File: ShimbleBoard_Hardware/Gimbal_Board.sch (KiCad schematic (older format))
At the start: 84 parts, among them Q1 Q_NMOS_GDS, Q2 Q_NMOS_GDS, Q3 Q_NMOS_GDS, Q4 Q_NMOS_GDS, Q5 Q_NMOS_GDS, Q6 Q_NMOS_GDS, Q7 Q_NMOS_GDS, Q8 Q_NMOS_GDS, SW1 SW_Push, SW10 SW_SPDT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

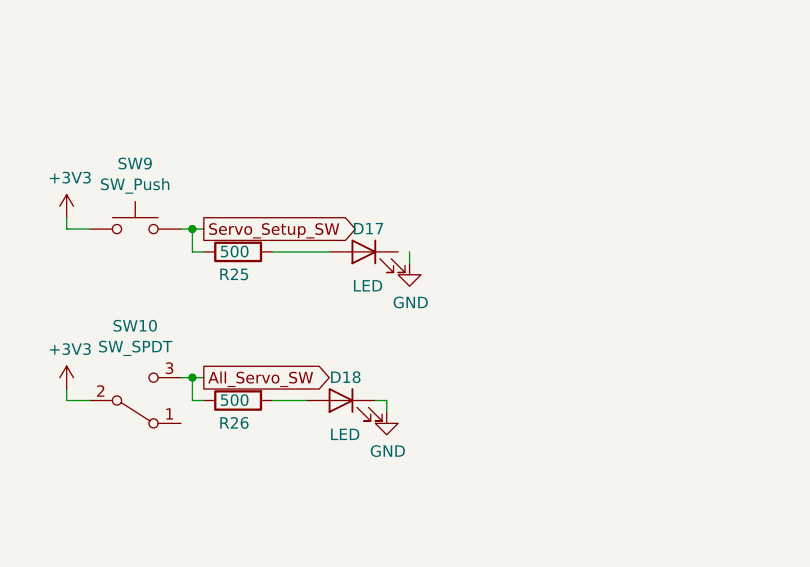
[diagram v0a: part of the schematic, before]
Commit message: PCB placement (not finished
PCB component placement and wiring
Still needs a lot more work, button pins need to be determined
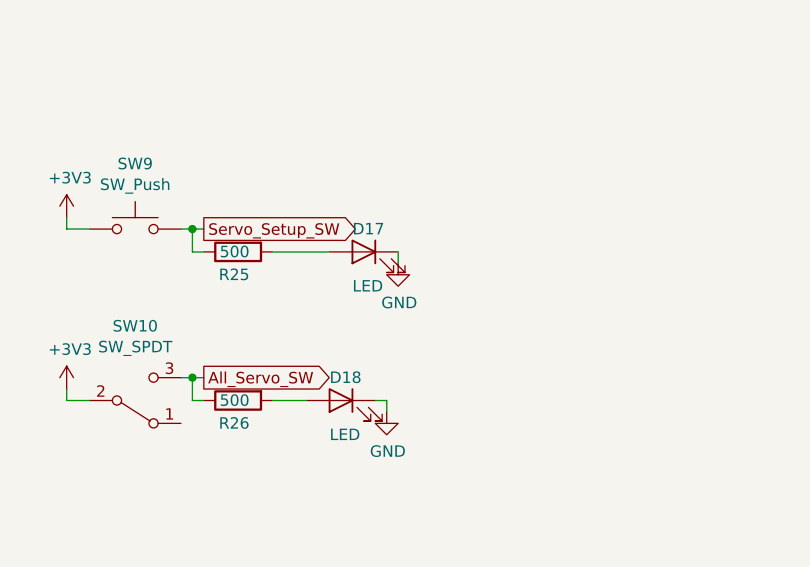
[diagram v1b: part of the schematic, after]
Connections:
- net GND: now also D17.1 (K)
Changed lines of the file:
@@
 	-1   0    0    -1
 $EndComp
-Text GLabel 3500 4900 0    50   Output ~ 0
-Servo_Ctrl_7
-Text GLabel 3500 5000 0    50   Output ~ 0
-Servo_Ctrl_8
 $Comp
 L power:GND #PWR0107
@@
 Text GLabel 1350 4750 0    50   Output ~ 0
 Servo_Ctrl_1
-Text GLabel 1350 4850 0    50   Output ~ 0
-Servo_Ctrl_2
 Text GLabel 1350 4950 0    50   Output ~ 0
 Servo_Ctrl_3
-Text GLabel 1350 5050 0    50   Output ~ 0
-Servo_Ctrl_4
 Text GLabel 7250 2100 3    50   Input ~ 0
 Servo_Ctrl_1
@@
 Text Notes 550  4800 0    50   ~ 0
 PWM 1
-Text Notes 550  4900 0    50   ~ 0
-PWM 2
 Text Notes 550  5000 0    50   ~ 0
 PWM 3
-Text Notes 550  5100 0    50   ~ 0
-PWM 4
 Wire Wire Line
 	3550 5000 3500 5000
@@
 L power:GND #PWR0128
 U 1 1 5DC2F611
-P 7550 10200
-F 0 "#PWR0128" H 7550 9950 50  0001 C CNN
-F 1 "GND" H 7555 10027 50  0000 C CNN
-F 2 "" H 7550 10200 50  0001 C CNN
-F 3 "" H 7550 10200 50  0001 C CNN
-	1    7550 10200
+P 7500 10200
+F 0 "#PWR0128" H 7500 9950 50  0001 C CNN
+F 1 "GND" H 7505 10027 50  0000 C CNN
+F 2 "" H 7500 10200 50  0001 C CNN
+F 3 "" H 7500 10200 50  0001 C CNN
+	1    7500 10200
 	1    0    0    -1
 $EndComp
@@
 Text GLabel 6650 10050 2    50   Output ~ 0
 Servo_Setup_SW
-Text GLabel 4400 11550 2    50   Output ~ 0
-Servo_SW_8
 Text GLabel 4400 11200 2    50   Output ~ 0
 Servo_SW_7
@@
 	6600 10050 6550 10050
 Wire Wire Line
-	7550 10150 7550 10200
+	7500 10150 7500 10200
 Wire Wire Line
 	7450 10850 7450 10800
@@
 	0    1    1    0
 $EndComp
+Text Notes 550  5100 0    50   ~ 0
+PWM 4
+Text Notes 550  4900 0    50   ~ 0
+PWM 2
+Text GLabel 1350 5050 0    50   Output ~ 0
+Servo_Ctrl_4
+Text GLabel 1350 4850 0    50   Output ~ 0
+Servo_Ctrl_2
+Text GLabel 3500 4900 0    50   Output ~ 0
+Servo_Ctrl_7
+Text GLabel 3500 5000 0    50   Output ~ 0
+Servo_Ctrl_8
+Text GLabel 4400 11550 2    50   Output ~ 0
+Servo_SW_8
 $EndSCHEMATC

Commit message: Cleaned some stuff
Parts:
- added C?: 470u, Capacitor_THT:CP_Radial_D8.0mm_P3.50mm, symbol Device:CP1
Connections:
- net +5VA: now also C?.1
- net GND: now also C?.2
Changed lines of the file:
@@
 Comment4 ""
 $EndDescr
-Connection ~ 3850 2100
-Wire Wire Line
-	3850 2050 3850 2100
 Connection ~ 3850 2500
 Wire Wire Line
-	3850 2500 3850 2550
+	4250 2500 4250 2550
 Connection ~ 2950 2500
 Wire Wire Line
@@
 Wire Wire Line
 	3850 2450 3850 2500
-Connection ~ 3400 2100
-Wire Wire Line
-	3850 2100 3850 2150
-Wire Wire Line
-	3400 2100 3850 2100
 Connection ~ 2950 2100
 Wire Wire Line
@@
 L power:+5VA #PWR07
 U 1 1 5DAD4728
-P 3850 2050
-F 0 "#PWR07" H 3850 1900 50  0001 C CNN
-F 1 "+5VA" H 3865 2223 50  0000 C CNN
-F 2 "" H 3850 2050 50  0001 C CNN
-F 3 "" H 3850 2050 50  0001 C CNN
-	1    3850 2050
-	1    0    0    -1
-$EndComp
-$Comp
-L power:GND #PWR08
-U 1 1 5DAD3C4F
-P 3850 2550
-F 0 "#PWR08" H 3850 2300 50  0001 C CNN
-F 1 "GND" H 3855 2377 50  0000 C CNN
-F 2 "" H 3850 2550 50  0001 C CNN
-F 3 "" H 3850 2550 50  0001 C CNN
-	1    3850 2550
+P 4250 2050
+F 0 "#PWR07" H 4250 1900 50  0001 C CNN
+F 1 "+5VA" H 4265 2223 50  0000 C CNN
+F 2 "" H 4250 2050 50  0001 C CNN
+F 3 "" H 4250 2050 50  0001 C CNN
+	1    4250 2050
 	1    0    0    -1
 $EndComp
@@
 $EndComp
 Wire Notes Line
-	4200 500  4200 2800
+	4600 500  4600 2800
 Text Notes 7350 7500 0    69   ~ 14
 Shimble Board
@@
 	500  800  1850 800
 Wire Notes Line
-	4200 500  1900 500
-Wire Notes Line
-	4200 2800 1900 2800
-Wire Notes Line
 	1900 2800 1900 500
-Wire Notes Line
-	4200 800  1900 800
 Text Notes 17300 7500 0    50   ~ 0
 Orange
@@
 Text GLabel 4400 11550 2    50   Output ~ 0
 Servo_SW_8
+Wire Wire Line
+	4250 2450 4250 2500
+$Comp
+L Device:CP1 C?
+U 1 1 5DD2ACC6
+P 4250 2300
+F 0 "C?" H 4365 2346 50  0000 L CNN
+F 1 "470u" H 4365 2255 50  0000 L CNN
+F 2 "Capacitor_THT:CP_Radial_D8.0mm_P3.50mm" H 4250 2300 50  0001 C CNN
+F 3 "~" H 4250 2300 50  0001 C CNN
+	1    4250 2300
+	1    0    0    -1
+$EndComp
+Connection ~ 3400 2100
+Wire Wire Line
+	3400 2100 3850 2100
+Wire Wire Line
+	3850 2100 3850 2150
+Wire Wire Line
+	4250 2050 4250 2100
+Connection ~ 3850 2100
+Wire Wire Line
+	4250 2100 4250 2150
+Wire Wire Line
+	4250 2100 3850 2100
+Wire Wire Line
+	4250 2500 3850 2500
+Connection ~ 4250 2100
+$Comp
+L power:GND #PWR08
+U 1 1 5DAD3C4F
+P 4250 2550
+F 0 "#PWR08" H 4250 2300 50  0001 C CNN
+F 1 "GND" H 4255 2377 50  0000 C CNN
+F 2 "" H 4250 2550 50  0001 C CNN
+F 3 "" H 4250 2550 50  0001 C CNN
+	1    4250 2550
+	1    0    0    -1
+$EndComp
+Connection ~ 4250 2500
+Wire Notes Line
+	1900 2800 4600 2800
+Wire Notes Line
+	1900 800  4600 800
+Wire Notes Line
+	1900 500  4600 500
 $EndSCHEMATC

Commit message: Cleaned
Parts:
- gave numbers to parts that had none: 1
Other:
- note added: "Servo Buttons"
- note added: "Servo Switches"
- moved on the sheet: C1, C2, C3, C4, C5, C6, C7, Conn1, Conn2, Conn3, Conn4, Conn5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

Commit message: Fixed stuff
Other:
- note added: "All Servo"
- note removed: "Servo Switches"
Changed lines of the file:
@@
 Text Notes 7600 750  0    138  Italic 28
 Servo Buttons
-Text Notes 9400 750  0    138  Italic 28
-Servo Switches
+Text Notes 9750 750  0    138  Italic 28
+All Servo
 $EndSCHEMATC
